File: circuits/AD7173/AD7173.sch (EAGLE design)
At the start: 37 parts, among them IC1 AD7173, IC2 ADP1720, IC3 ADP1720ARMZ-5, IC4 ADR445BR, Q1 FA-20H

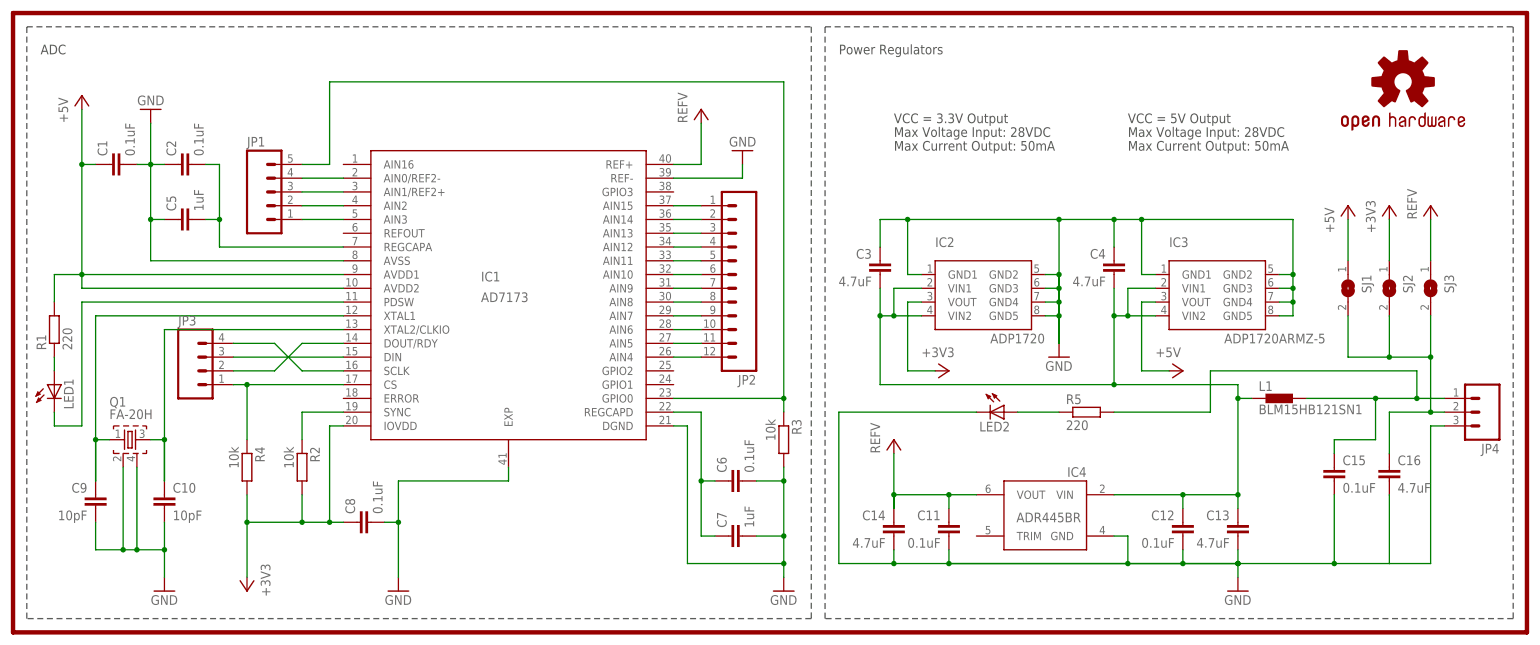
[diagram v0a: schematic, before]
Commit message: Fixed some ERC errors, approved others. Caught some missing dots and duplicate wire segments. Added dummy value "." to devices where ERC requires value. Color might be more informative value for LEDs. It would be better to resolve I/O mapping conflicts than to approve ERC errors.
Signed-off-by: Christoph Maier <cm.hardware.software.elsewhere@gmail.com>
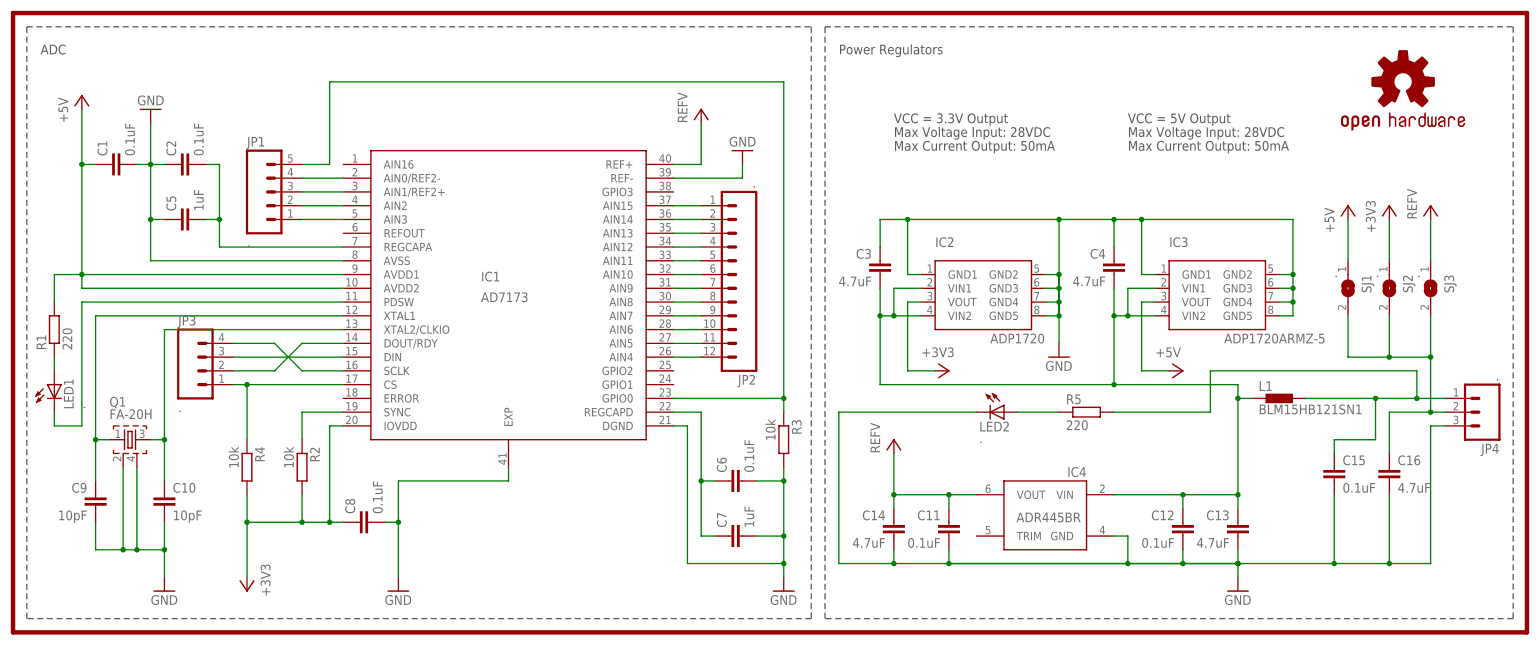
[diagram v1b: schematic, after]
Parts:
- JP1, JP2, JP3, JP4, LED1, LED2, SJ1, SJ2, SJ3: value (none) -> .
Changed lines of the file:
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@@
 <?xml version="1.0" encoding="utf-8"?>
 <!DOCTYPE eagle SYSTEM "eagle.dtd">
-<eagle version="7.4.0">
+<eagle version="6.5.0">
 <drawing>
 <settings>
@@
 <part name="GND1" library="supply1" deviceset="GND" device=""/>
 <part name="R1" library="rcl" deviceset="R-EU_" device="R0402" value="220"/>
-<part name="LED1" library="led" deviceset="LED" device="CHIP-LED0603"/>
+<part name="LED1" library="led" deviceset="LED" device="CHIP-LED0603" value="."/>
 <part name="C1" library="rcl" deviceset="C-EU" device="C0402" value="0.1uF"/>
 <part name="R2" library="rcl" deviceset="R-EU_" device="R0402" value="10k"/>
@@
 <part name="C15" library="rcl" deviceset="C-EU" device="C0402" value="0.1uF"/>
 <part name="P+4" library="supply1" deviceset="+5V" device=""/>
-<part name="SJ1" library="jumper" deviceset="SJ" device=""/>
-<part name="SJ2" library="jumper" deviceset="SJ" device=""/>
-<part name="SJ3" library="jumper" deviceset="SJ" device=""/>
+<part name="SJ1" library="jumper" deviceset="SJ" device="" value="."/>
+<part name="SJ2" library="jumper" deviceset="SJ" device="" value="."/>
+<part name="SJ3" library="jumper" deviceset="SJ" device="" value="."/>
 <part name="P+5" library="supply1" deviceset="+5V" device=""/>
 <part name="+3V3" library="supply1" deviceset="+3V3" device=""/>
 <part name="P+6" library="supply1" deviceset="VCC" device="" value="REFV"/>
-<part name="LED2" library="led" deviceset="LED" device="CHIP-LED0603"/>
+<part name="LED2" library="led" deviceset="LED" device="CHIP-LED0603" value="."/>
 <part name="R5" library="rcl" deviceset="R-EU_" device="R0402" value="220"/>
 <part name="C16" library="rcl" deviceset="C-EU" device="C0402" value="4.7uF"/>
 <part name="LOGO1" library="SparkFun-Aesthetics" deviceset="OSHW-LOGO" device="S"/>
-<part name="JP1" library="SparkFun-Connectors" deviceset="M05" device="PTH"/>
-<part name="JP2" library="SparkFun-Connectors" deviceset="M12" device="PTH"/>
-<part name="JP3" library="SparkFun-Connectors" deviceset="M04" device="PTH"/>
-<part name="JP4" library="SparkFun-Connectors" deviceset="M03" device="PTH"/>
+<part name="JP1" library="SparkFun-Connectors" deviceset="M05" device="PTH" value="."/>
+<part name="JP2" library="SparkFun-Connectors" deviceset="M12" device="PTH" value="."/>
+<part name="JP3" library="SparkFun-Connectors" deviceset="M04" device="PTH" value="."/>
+<part name="JP4" library="SparkFun-Connectors" deviceset="M03" device="PTH" value="."/>
 </parts>
 <sheets>
@@
 <wire x1="261.62" y1="38.1" x2="264.16" y2="38.1" width="0.1524" layer="91"/>
 <pinref part="JP4" gate="G$1" pin="3"/>
+<junction x="254" y="12.7"/>
 </segment>
 <segment>
@@
 <junction x="193.04" y="58.42"/>
 <wire x1="203.2" y1="76.2" x2="193.04" y2="76.2" width="0.1524" layer="91"/>
-<wire x1="193.04" y1="66.04" x2="193.04" y2="53.34" width="0.1524" layer="91"/>
 <junction x="193.04" y="76.2"/>
 <junction x="203.2" y="76.2"/>
@@
 <pinref part="C10" gate="G$1" pin="1"/>
 <pinref part="Q1" gate="G$1" pin="3"/>
-<wire x1="27.94" y1="35.56" x2="27.94" y2="27.94" width="0.1524" layer="91"/>
 <wire x1="25.4" y1="35.56" x2="27.94" y2="35.56" width="0.1524" layer="91"/>
 <wire x1="27.94" y1="35.56" x2="27.94" y2="27.94" width="0.1524" layer="91"/>
@@
 <wire x1="15.24" y1="35.56" x2="15.24" y2="27.94" width="0.1524" layer="91"/>
 <wire x1="17.78" y1="35.56" x2="15.24" y2="35.56" width="0.1524" layer="91"/>
-<wire x1="15.24" y1="35.56" x2="15.24" y2="27.94" width="0.1524" layer="91"/>
 <junction x="15.24" y="35.56"/>
 </segment>
@@
 <pinref part="P+1" gate="VCC" pin="VCC"/>
 <wire x1="172.72" y1="25.4" x2="177.8" y2="25.4" width="0.1524" layer="91"/>
-<wire x1="162.56" y1="22.86" x2="162.56" y2="25.4" width="0.1524" layer="91"/>
 <junction x="162.56" y="25.4"/>
 <wire x1="162.56" y1="25.4" x2="162.56" y2="33.02" width="0.1524" layer="91"/>
@@
 </sheet>
 </sheets>
+<errors>
+</errors>
 </schematic>
 </drawing>
